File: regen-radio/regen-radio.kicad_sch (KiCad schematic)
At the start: 47 parts, among them P1 POTWS20, Q1 2N2219, Q2 2N2219, T1 Antenna-TICKLE-SS, T2 Transformer_1P_1S, U1 LM386

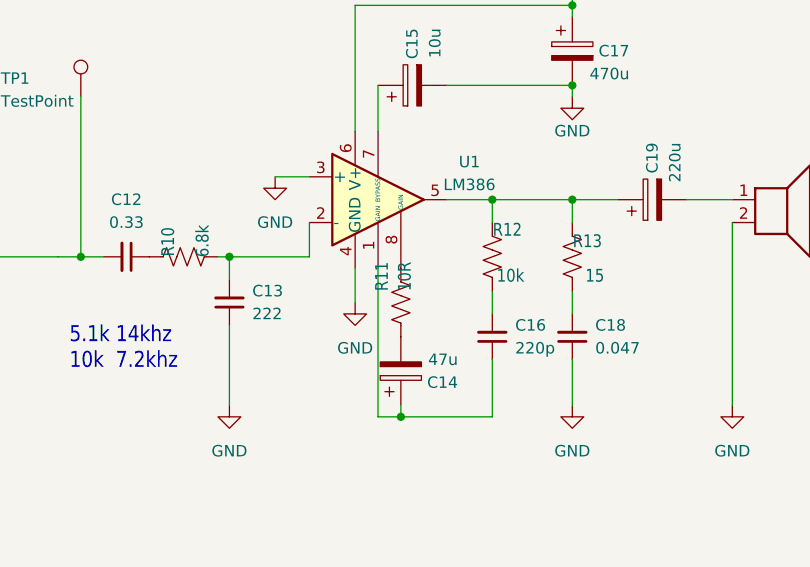
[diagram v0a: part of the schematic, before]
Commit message: feat(regen-radio): add sch meta
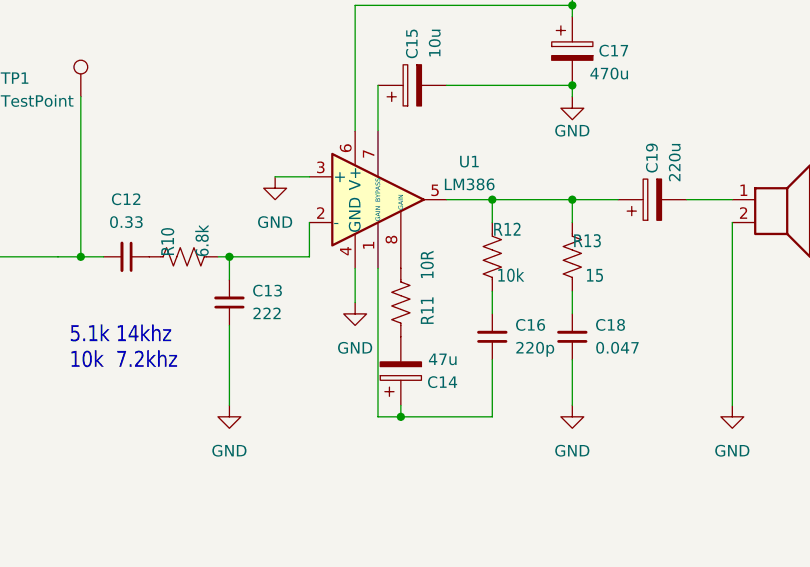
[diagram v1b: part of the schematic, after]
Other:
- company: (none) -> µHenry Radio Club
- title: (none) -> Regen Radio
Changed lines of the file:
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@@
 (kicad_sch (version 20230121) (generator eeschema)
   (paper "A4")
+  (title_block
+    (title "Regen Radio")
+    (date "2024-01-28")
+    (rev "0.0.1")
+    (company "µHenry Radio Club")
+  )
   (junction (at 154.94 85.09) (diameter 0) (color 0 0 0 0)
   )
@@
   (symbol (lib_id "Device:R_US") (at 214.63 90.17 180) (unit 1)
     (in_bom yes) (on_board yes) (dnp no)
-    (property "Reference" "R11" (at 213.36 88.9 90)
-      (effects (font (size 1.4224 1.209)) (justify right top))
-    )
-    (property "Value" "10R" (at 215.9 88.9 90)
-      (effects (font (size 1.4224 1.209)) (justify right top))
-    )
+    (property "Reference" "R11" (at 218.44 92.71 90)
+      (effects (font (size 1.4224 1.209)) (justify right top))
+    )
+    (property "Value" "10R" (at 218.44 87.63 90)
+      (effects (font (size 1.4224 1.209)) (justify right top))
+    )
